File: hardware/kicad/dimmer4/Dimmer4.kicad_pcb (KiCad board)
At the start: 2 copper layers, 64 x 60 mm, 45 parts, among them J100 Stapelstecker 2x20, J101 Kettenstecker, Buchse oben (S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, J102 Kettenstecker, Stift unten (S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, J103 Leistungsstecker, Buchse oben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, J104 Leistungsstecker, Stift unten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, J5 LED-Kanal 1, J6 LED-Kanal 2, J7 LED-Kanal 3, J8 LED-Kanal 4, Q1 NCE6050KA, Q10 IRFR5305, Q2 NCE6050KA, Q3 NCE6050KA, Q4 NCE6050KA, U100 STM32C011F6P6, U101 SN74LVC1G175, U102 SN74LVC2G00DCUR, U103 SN74LVC1G08

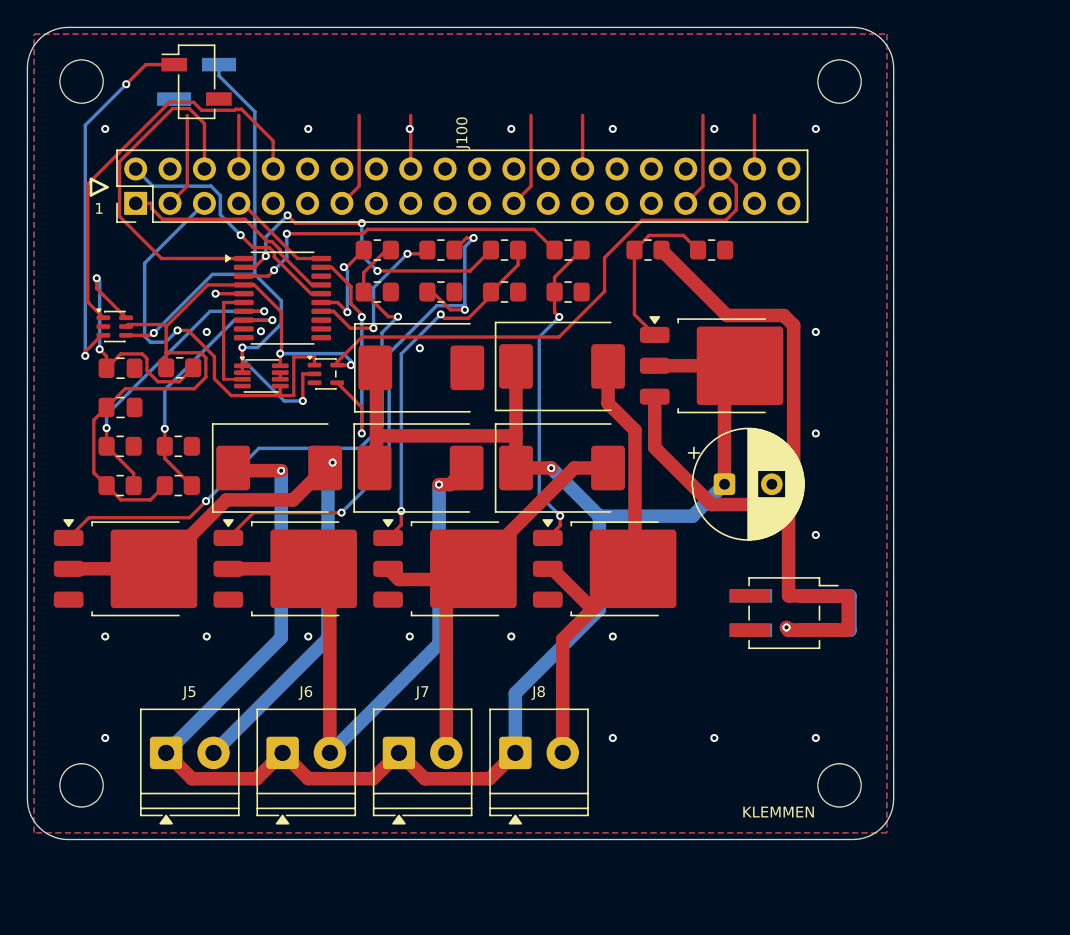
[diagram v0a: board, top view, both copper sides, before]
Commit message: Aufgabe 8b: Dimmer4 verlegt -- 0 Verletzungen, 0 offene Posten
Wurf f4_6 (sechster Wurf der dritten Serie, gebaut aus dem Stand von
e51a338). Kette wie beim Motormodul: bauen -> Vorverdrahtungs-Gate
(0 Verletzungen ohne Router) -> autoroute -> masseheiler -> DRC.

  kicad-cli pcb drc --severity-error --exit-code-violations
    Found 0 violations
    Found 0 unconnected items
  masseheiler --nur-pruefen
    alle Masseflaechen haengen zusammen, nichts zu tun
  steckerprobe spec_dimmer4
    alle elf Zeilen gruen, "Stecker sitzen auf der Vertragslage."
  pcb_checks
    Vias: 71, alle beidseitig angebunden
    ANTENNE_FREI (29.0..50.0 x 42.9..51.9): F.Cu kupferfrei

Der Router liess in diesem Wurf keine Verbindung offen; masseheiler
heilte drei Gussfragmente ueber einfache Vias. Die in Aufgabe 8a
angemeldete Sorge um Kanal 4 (Diode und FET nebeneinander statt
uebereinander, laengerer Weg) hat sich nicht bestaetigt: keine
Verbindung der Kanal-4-Zone blieb in irgendeinem der 14 Dimmer4-Wuerfe
offen.

Co-Authored-By: Claude Fable 5 <noreply@anthropic.com>
Claude-Session: https://claude.ai/code/session_01KDus95JJwCeRuwccgBWEi5
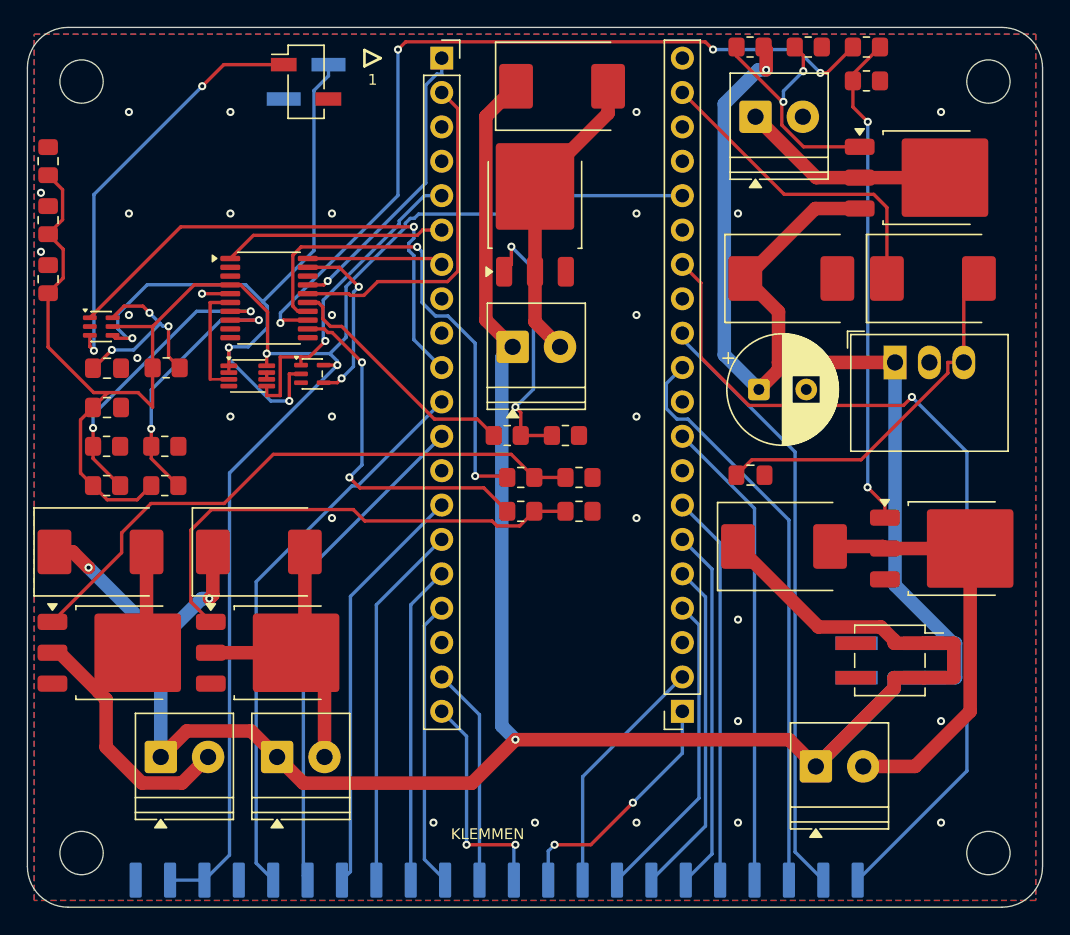
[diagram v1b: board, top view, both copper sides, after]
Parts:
- removed C12: 220u, CP_Radial_D8.0mm_P3.50mm
- removed D10: SMCJ30A, D_SMC
- removed Q10: IRFR5305, TO-252-3_TabPin2
- removed R11, R12: 10k, R_0805_2012Metric_Pad1.20x1.40mm_HandSolder
- added C102: 100n, C_0805_2012Metric_Pad1.18x1.45mm_HandSolder, F.Cu at (1.53, 9.88)
- added C103: 100n, C_0805_2012Metric_Pad1.18x1.45mm_HandSolder, F.Cu at (1.53, 14.2)
- added C104: 100n, C_0805_2012Metric_Pad1.18x1.45mm_HandSolder, F.Cu at (1.53, 18.6)
- added C90: 220u, CP_Radial_D8.0mm_P3.50mm, F.Cu at (54.0, 26.8)
- added C91: 22u, C_0805_2012Metric_Pad1.18x1.45mm_HandSolder, F.Cu at (53.4, 33.1)
- added D90: SMCJ30A, D_SMC, F.Cu at (56.4, 18.6)
- added D91: SS36C, D_SMC, F.Cu at (66.9, 18.6)
- added J105: Stapelstecker rechts, Pico-Pins 21..40 (Buchse), PinSocket_1x20_P2.54mm_Vertical, F.Cu at (48.4, 50.5)
- added J90: Versorgung Eingang, TerminalBlock_Phoenix_PT-1,5-2-3.5-H_1x02_P3.50mm_Horizontal, F.Cu at (53.8, 6.60)
- added J95: Randpads GPIO, unbestueckt (THT-Loetpad), Randpad_Reihe_1x18, B.Cu at (18.2, 63.0)
- added J96: Randpads Versorgung: 2x 3V3 + 2x GND, unbestueckt (THT-Loet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, Randpad_Reihe_1x04, B.Cu at (8.00, 63.0)
- added Q90: IRFR5305, TO-252-3_TabPin2, F.Cu at (66.5, 11.1)
- added R90: 10k, R_0805_2012Metric_Pad1.20x1.40mm_HandSolder, F.Cu at (53.4, 1.45)
- added R91: 10k, R_0805_2012Metric_Pad1.20x1.40mm_HandSolder, F.Cu at (57.7, 1.45)
- added U90: K7805-1000R3, Converter_DCDC_RECOM_R-78B-2.0_THT, F.Cu at (64.1, 24.8)
- D1, D2, D3, D4: value SS36 -> SS36C
- J100: value Stapelstecker 2x20 -> Stapelstecker links, Pico-Pins 1..20 (Buchse); footprint PinHeader_2x20_P2.54mm_Vertical -> PinSocket_1x20_P2.54mm_Vertical
- Q1, Q2, Q3, Q4: value NCE6050KA -> NCE6020AK
- moved Q1 39.9 mm to (37.5, 13.0), turned to 90 degrees
- moved J5 39.4 mm to (35.9, 23.6)
- moved D1 35.1 mm to (39.5, 4.35)
- moved RP4 27.0 mm to (62.0, 3.95)
- moved RG4 26.7 mm to (62.0, 1.45)
- moved J100 25.0 mm to (30.6, 2.27), turned to 0 degrees
- moved Q4 24.9 mm to (68.4, 38.5)
- moved D2 24.4 mm to (5.40, 38.8)
- moved D3 23.2 mm to (17.1, 38.8)
- moved J8 22.2 mm to (58.2, 54.6)
- moved D4 21.1 mm to (55.9, 38.4)
- moved RG3 19.3 mm to (36.5, 35.8)
- moved RG2 17.8 mm to (36.5, 33.2)
- moved RP1 17.5 mm to (39.8, 30.1)
- moved RP3 17.1 mm to (40.8, 35.8)
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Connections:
- J100 pad 11: unconnected-(J100-Pin_11-Pad11) -> /GP8
- J100 pad 12: unconnected-(J100-Pin_12-Pad12) -> /GP9
- J100 pad 14: unconnected-(J100-Pin_14-Pad14) -> /GP10
- J100 pad 15: unconnected-(J100-Pin_15-Pad15) -> /GP11
- J100 pad 16: unconnected-(J100-Pin_16-Pad16) -> /GP12
- J100 pad 17: unconnected-(J100-Pin_17-Pad17) -> /GP13
- J100 pad 19: unconnected-(J100-Pin_19-Pad19) -> /GP14
- J100 pad 20: unconnected-(J100-Pin_20-Pad20) -> /GP15
- J103 pad 1: /PWR24V -> /+24V
- J103 pad 3: /PWR24V -> /+24V
- J104 pad 1: /PWR24V -> /+24V
- J104 pad 3: /PWR24V -> /+24V
- U100 pad 10: /IN2 -> unconnected-(U100-PA3-Pad10)
- U100 pad 11: /NSLEEP -> unconnected-(U100-PA4-Pad11)
- U100 pad 12: /NFAULT -> /PWM3
- U100 pad 13: /IPROPI -> /PWM4
- U100 pad 2: /PWM3 -> unconnected-(U100-PC14-Pad2)
- U100 pad 3: /PWM4 -> unconnected-(U100-PC15-Pad3)
- U100 pad 9: /IN1 -> unconnected-(U100-PA2-Pad9)
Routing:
- net /+24V: track 136.6 -> 264.2 mm, vias 2 -> 4
- net /PWR24V: track 68.9 -> 0.00 mm, vias 1 -> 0
- net /GP28: track 0.00 -> 65.5 mm, vias 0 -> 1
- net 3V3: track 91.4 -> 145.5 mm
- net /GP27: track 0.00 -> 44.7 mm
- net GND: track 46.0 -> 2.09 mm, vias 24 -> 29
- net /GP26: track 0.00 -> 42.6 mm
- net /GP8: track 0.00 -> 41.8 mm
- net /GP9: track 0.00 -> 37.2 mm
- net /PWM4: track 26.1 -> 61.5 mm, vias 2 -> 4
- net /GP22: track 0.00 -> 35.0 mm
- net /GP10: track 0.00 -> 30.8 mm
- net /GP21: track 0.00 -> 28.9 mm
- net /+5V_LOKAL: track 0.00 -> 27.4 mm
- net /GP11: track 0.00 -> 27.2 mm
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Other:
- board size 64 x 60 mm -> 75 x 65 mm
